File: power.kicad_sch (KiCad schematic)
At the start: 27 parts, among them J3 Conn_01x03_Male, Q1 DMP1045U-7, Q2 UMW8205A, U1 XC6210B332MR, U2 TP4056M, U3 DW01A-G, U4 MAX17048G+T10

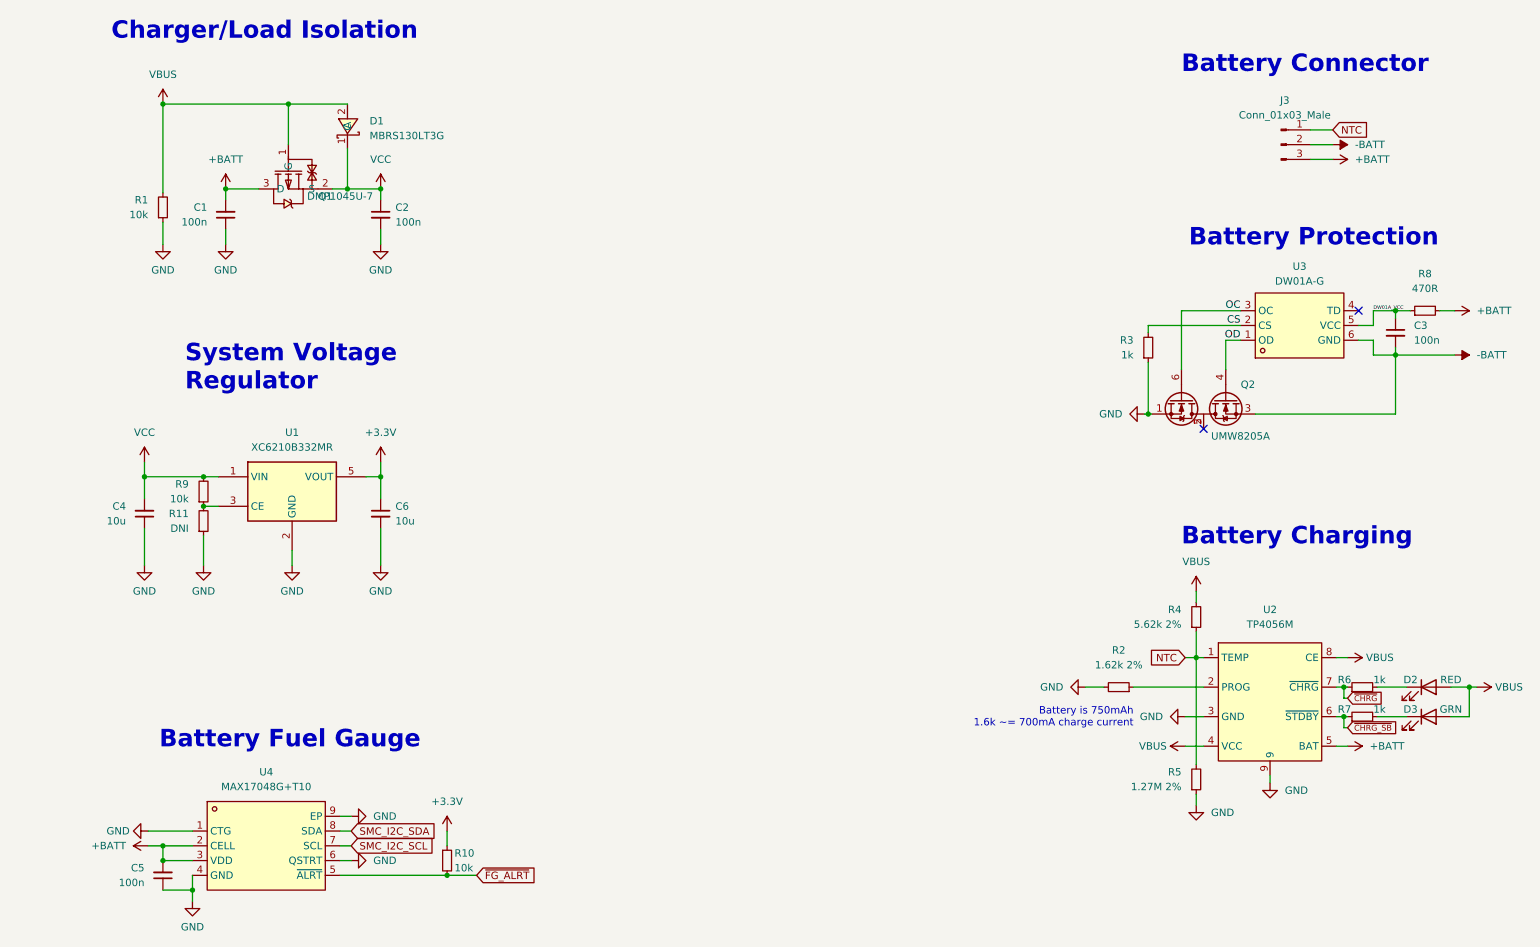
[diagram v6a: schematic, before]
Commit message: schem: migrate away from LCSC exclusive parts
- layout: migrate away from lcsc footprints
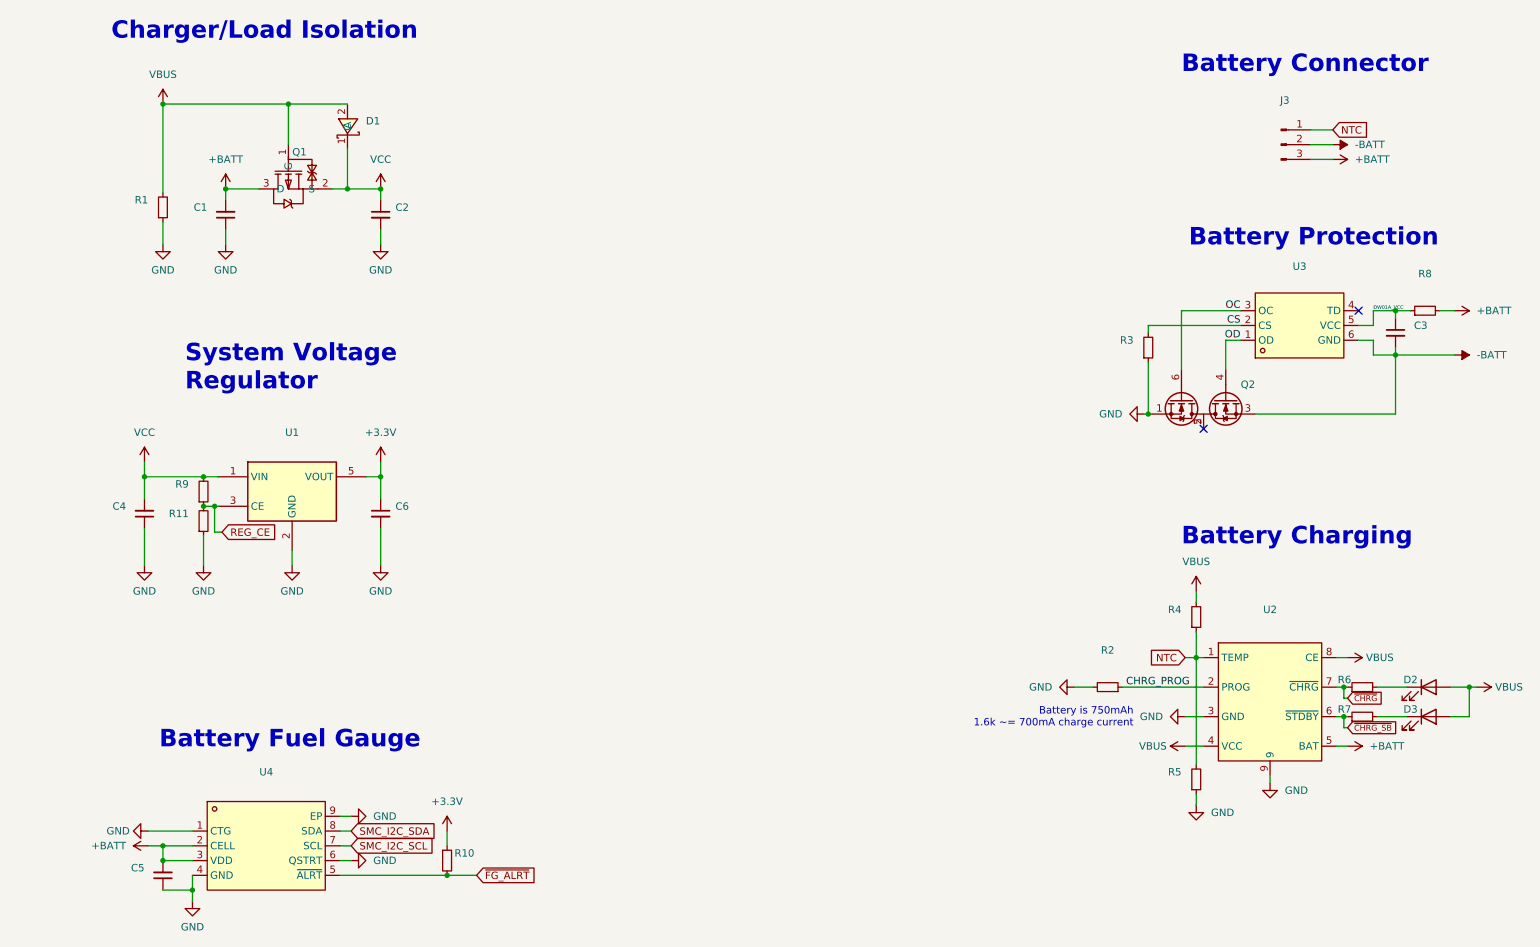
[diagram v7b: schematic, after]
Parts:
- C1, C2, C3, C5: value 100n -> (none); footprint Capacitor_SMD:C_0402_1005Metric -> (none)
- C4, C6: value 10u -> (none); footprint Capacitor_SMD:C_0402_1005Metric -> (none)
- D1: value MBRS130LT3G -> (none); footprint lcsc:SMB_L4.6-W3.6-LS5.3-RD -> (none); Digikey Part (none) -> MBRS130LT3GOSCT-ND; Digikey Price/Stock (none) -> https://www.digikey.com/en/products/detail/onsemi/MBRS130LT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; Manufacturer ON -> onsemi; Manufacturer Part (none) -> MBRS130LT3G; Mouser Part (none) -> 863-MBRS130LT3G; Mouser Price/Stock (none) -> https://www.mouser.ca/ProductDetail/onsemi/MBRS130LT3G?qs=3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
- D2: value RED -> (none); footprint LED_SMD:LED_0201_0603Metric -> (none)
- D3: value GRN -> (none); footprint LED_SMD:LED_0201_0603Metric -> (none)
- J3: value Conn_01x03_Male -> (none); footprint Gigahawk:Molex_PicoBlade_53047-0310_1x03_P1.25mm_Vertical -> (none); Digikey Part (none) -> WM1732-ND; Digikey Price/Stock (none) -> https://www.digikey.com/en/products/detail/molex/0530470310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; Manufacturer (none) -> MOLEX; Manufacturer Part (none) -> 0530470310
- Q1: value DMP1045U-7 -> (none); footprint lcsc:SOT-23-3_L2.9-W1.3-P1.90-LS2.4-BR -> (none); Digikey Part (none) -> DMP1045U-7DITR-ND; Digikey Price/Stock (none) -> https://www.digikey.com/en/products/detail/diodes-incorpora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; Manufacturer Part (none) -> DMP1045U-7; Mouser Part (none) -> 621-DMP1045U-7; Mouser Price/Stock (none) -> https://www.mouser.ca/ProductDetail/Diodes-Incorporated/DMP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
- Q2: value UMW8205A -> (none); footprint lcsc:SOT-23-6_L2.9-W1.6-P0.95-LS2.8-BL -> (none); Manufacturer Part (none) -> 8205A
- R1, R10, R9: value 10k -> (none); footprint Resistor_SMD:R_0402_1005Metric -> (none)
- R11: value DNI -> (none); footprint Resistor_SMD:R_0402_1005Metric -> (none)
- R2: value 1.62k 2% -> (none); footprint Resistor_SMD:R_0402_1005Metric -> (none)
- R3, R6, R7: value 1k -> (none); footprint Resistor_SMD:R_0402_1005Metric -> (none)
- R4: value 5.62k 2% -> (none); footprint Resistor_SMD:R_0402_1005Metric -> (none)
- R5: value 1.27M 2% -> (none); footprint Resistor_SMD:R_0402_1005Metric -> (none)
- R8: value 470R -> (none); footprint Resistor_SMD:R_0402_1005Metric -> (none)
- U1: value XC6210B332MR -> (none); footprint Package_TO_SOT_SMD:SOT-23-5 -> (none); Digikey Part (none) -> 893-1075-2-ND; Digikey Price/Stock (none) -> https://www.digikey.com/en/products/detail/torex-semiconduc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; JLC Part (none) -> Extended Part; LCSC Part (none) -> C47719; Manufacturer (none) -> Torex Semiconductor Ltd; Manufacturer Part (none) -> XC6210B332MR-G; Mouser Part (none) -> 865-XC6210B332MR-G; Mouser Price/Stock (none) -> https://www.mouser.ca/ProductDetail/Torex-Semiconductor/XC6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
- U2: value TP4056M -> (none); footprint lcsc:MSOP-8_L3.0-W3.0-P0.65-LS5.0-BL-EP -> (none); Manufacturer Part (none) -> TP4056M
- U3: value DW01A-G -> (none); footprint lcsc:SOT-23-6_L2.9-W1.6-P0.95-LS2.8-BR -> (none); Manufacturer Part (none) -> DW01A-G
- U4: value MAX17048G+T10 -> (none); footprint lcsc:DFN-8_L2.0-W2.0-P0.50-BL-EP -> (none); Digikey Part (none) -> MAX17048G+T10TR-ND; Digikey Price/Stock (none) -> https://www.digikey.com/en/products/detail/analog-devices-i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; Manufacturer MAXIM(美信) -> Maxim Integrated; Manufacturer Part (none) -> MAX17048G+T10; Mouser Part (none) -> 700-MAX17048G+T10; Mouser Price/Stock (none) -> https://www.mouser.ca/ProductDetail/Maxim-Integrated/MAX170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
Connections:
- net REG_CE: now reaches R11.2, R9.1, U1.3 (CE)
- net CHRG_PROG: now reaches R2.1, U2.2 (PROG)
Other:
- moved on the sheet: R2

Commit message: layout: update footprint for TP4056M
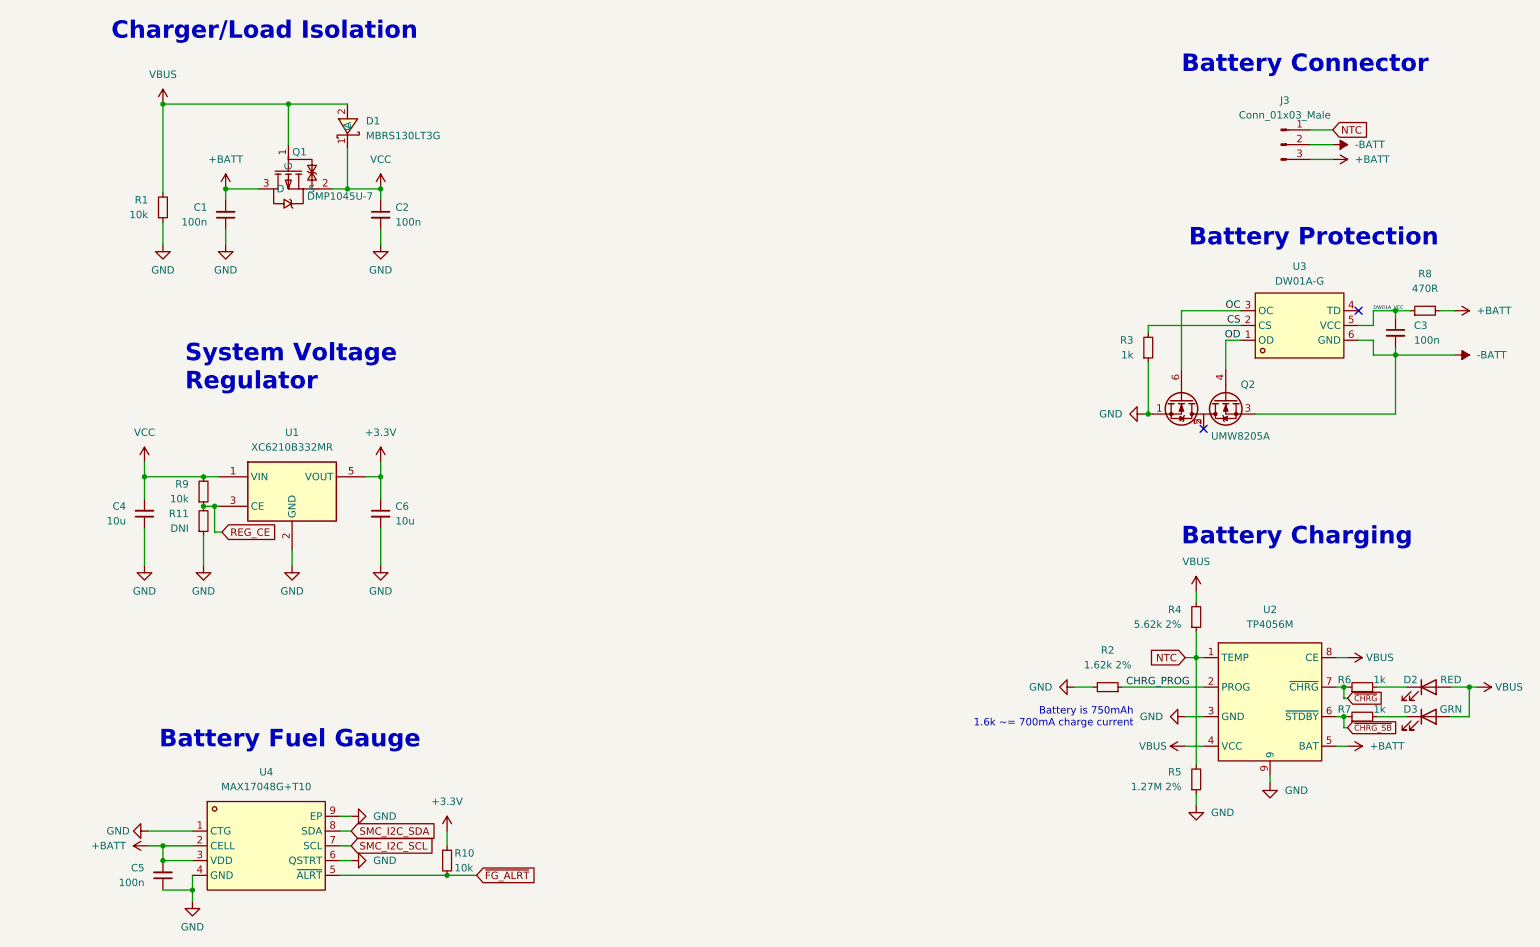
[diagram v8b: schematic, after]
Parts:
- C1, C2, C3, C5: value (none) -> 100n; footprint (none) -> Capacitor_SMD:C_0402_1005Metric
- C4, C6: value (none) -> 10u; footprint (none) -> Capacitor_SMD:C_0402_1005Metric
- D1: value (none) -> MBRS130LT3G; footprint (none) -> Diode_SMD:D_SMB
- D2: value (none) -> RED; footprint (none) -> LED_SMD:LED_0201_0603Metric
- D3: value (none) -> GRN; footprint (none) -> LED_SMD:LED_0201_0603Metric
- J3: value (none) -> Conn_01x03_Male; footprint (none) -> Gigahawk:Molex_PicoBlade_53047-0310_1x03_P1.25mm_Vertical
- Q1: value (none) -> DMP1045U-7; footprint (none) -> Package_TO_SOT_SMD:SOT-23
- Q2: value (none) -> UMW8205A; footprint (none) -> Package_TO_SOT_SMD:SOT-23-6
- R1, R10, R9: value (none) -> 10k; footprint (none) -> Resistor_SMD:R_0402_1005Metric
- R11: value (none) -> DNI; footprint (none) -> Resistor_SMD:R_0402_1005Metric
- R2: value (none) -> 1.62k 2%; footprint (none) -> Resistor_SMD:R_0402_1005Metric
- R3, R6, R7: value (none) -> 1k; footprint (none) -> Resistor_SMD:R_0402_1005Metric
- R4: value (none) -> 5.62k 2%; footprint (none) -> Resistor_SMD:R_0402_1005Metric
- R5: value (none) -> 1.27M 2%; footprint (none) -> Resistor_SMD:R_0402_1005Metric
- R8: value (none) -> 470R; footprint (none) -> Resistor_SMD:R_0402_1005Metric
- U1: value (none) -> XC6210B332MR; footprint (none) -> Package_TO_SOT_SMD:SOT-23-5
- U2: value (none) -> TP4056M; footprint (none) -> Gigahawk:MSOP-8-1EP_3x3mm_P0.65mm_EP1.425x1.76mm
- U3: value (none) -> DW01A-G; footprint (none) -> Package_TO_SOT_SMD:SOT-23-6
- U4: value (none) -> MAX17048G+T10; footprint (none) -> Package_DFN_QFN:DFN-8-1EP_2x2mm_P0.5mm_EP0.6x1.2mm
